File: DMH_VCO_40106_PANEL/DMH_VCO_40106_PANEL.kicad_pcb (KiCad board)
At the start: 2 copper layers, 100 x 200 mm, 35 parts, among them J1 GND

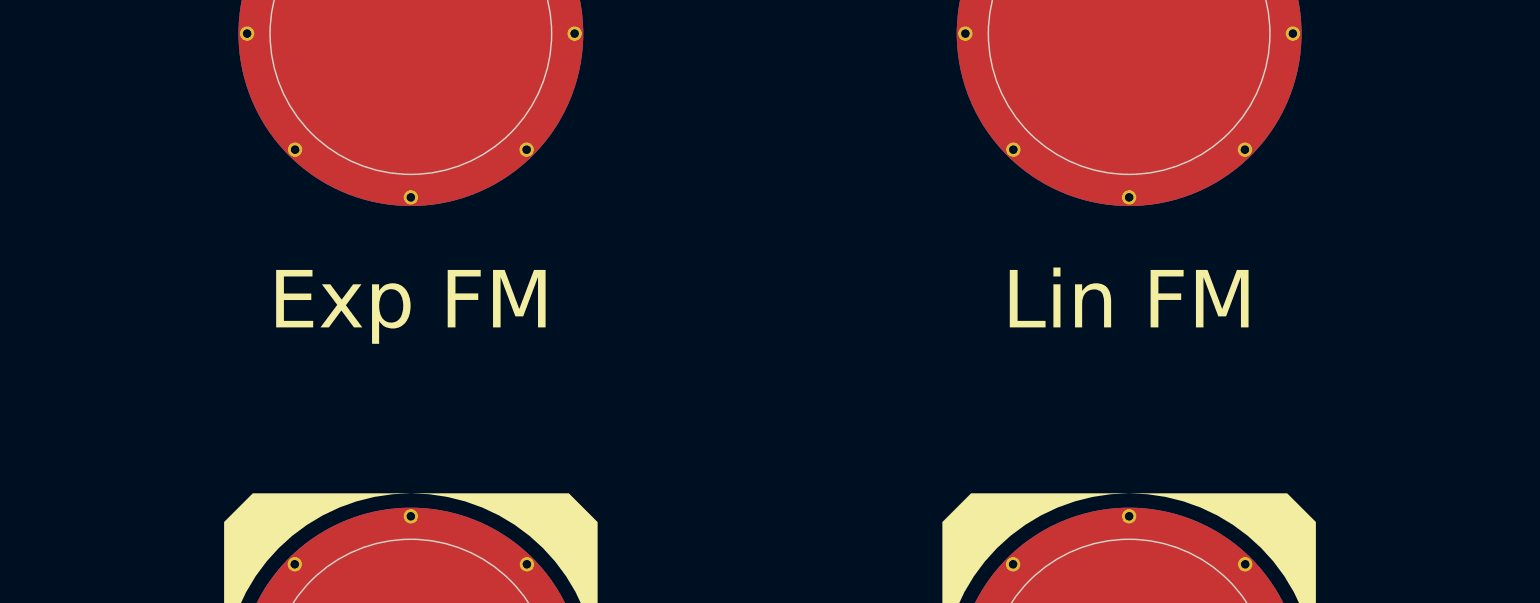
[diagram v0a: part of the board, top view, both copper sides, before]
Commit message: Updates from testing on breadboard
- Removed Bus CV input, normalled it to V/oct input jack instead
- Renamed Lin FM input to Exp FM In 2
- Added annotations about temporary resistor/pot values
- Added annotations about pots and trimpots pinout
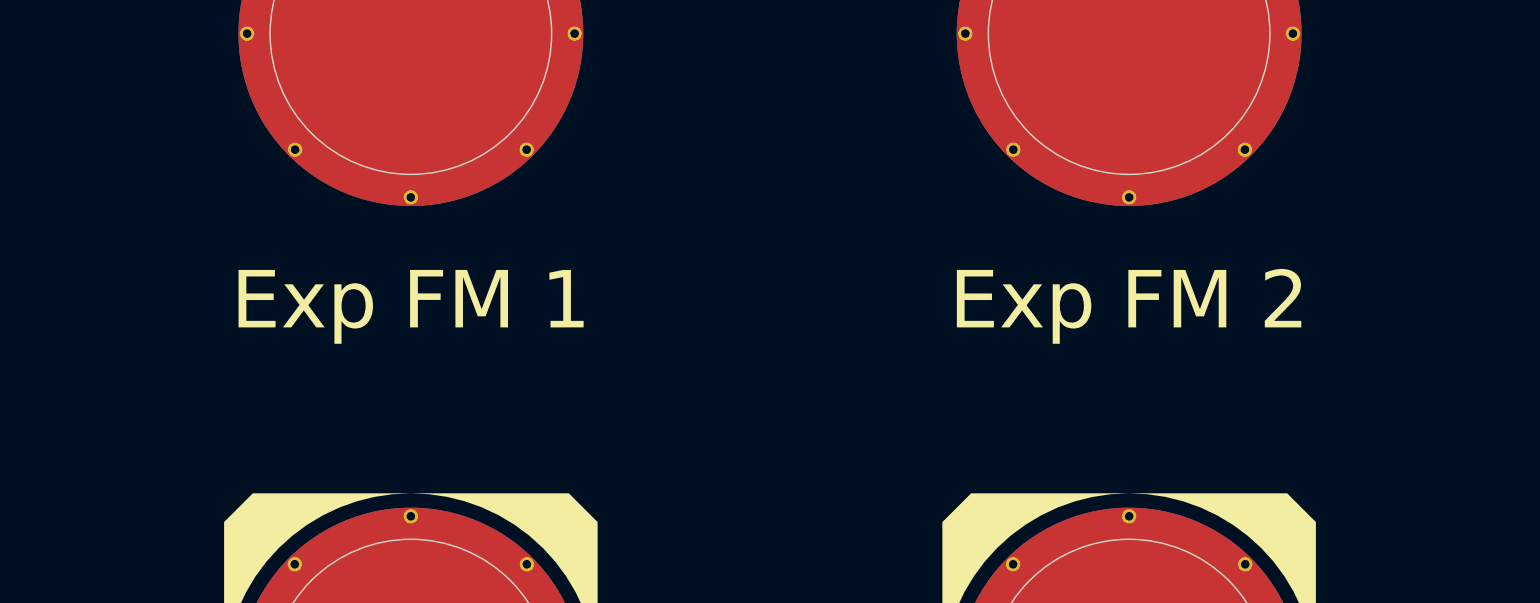
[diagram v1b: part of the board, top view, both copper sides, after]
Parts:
- H10, H18: value Exp FM -> Exp FM 1
- H11, H19: value Lin FM -> Exp FM 2

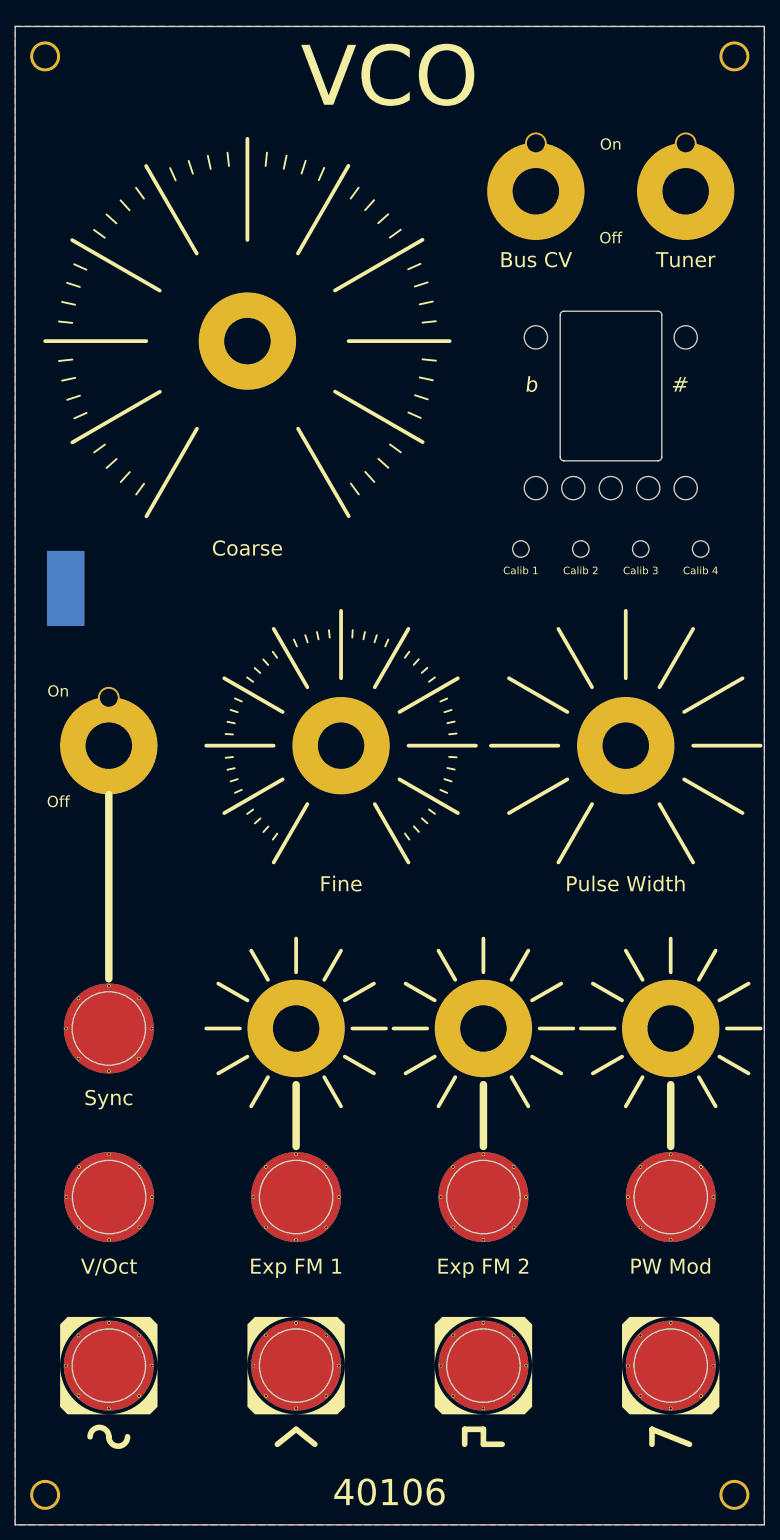
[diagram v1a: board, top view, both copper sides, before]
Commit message: Updated pot mounting hole sizes
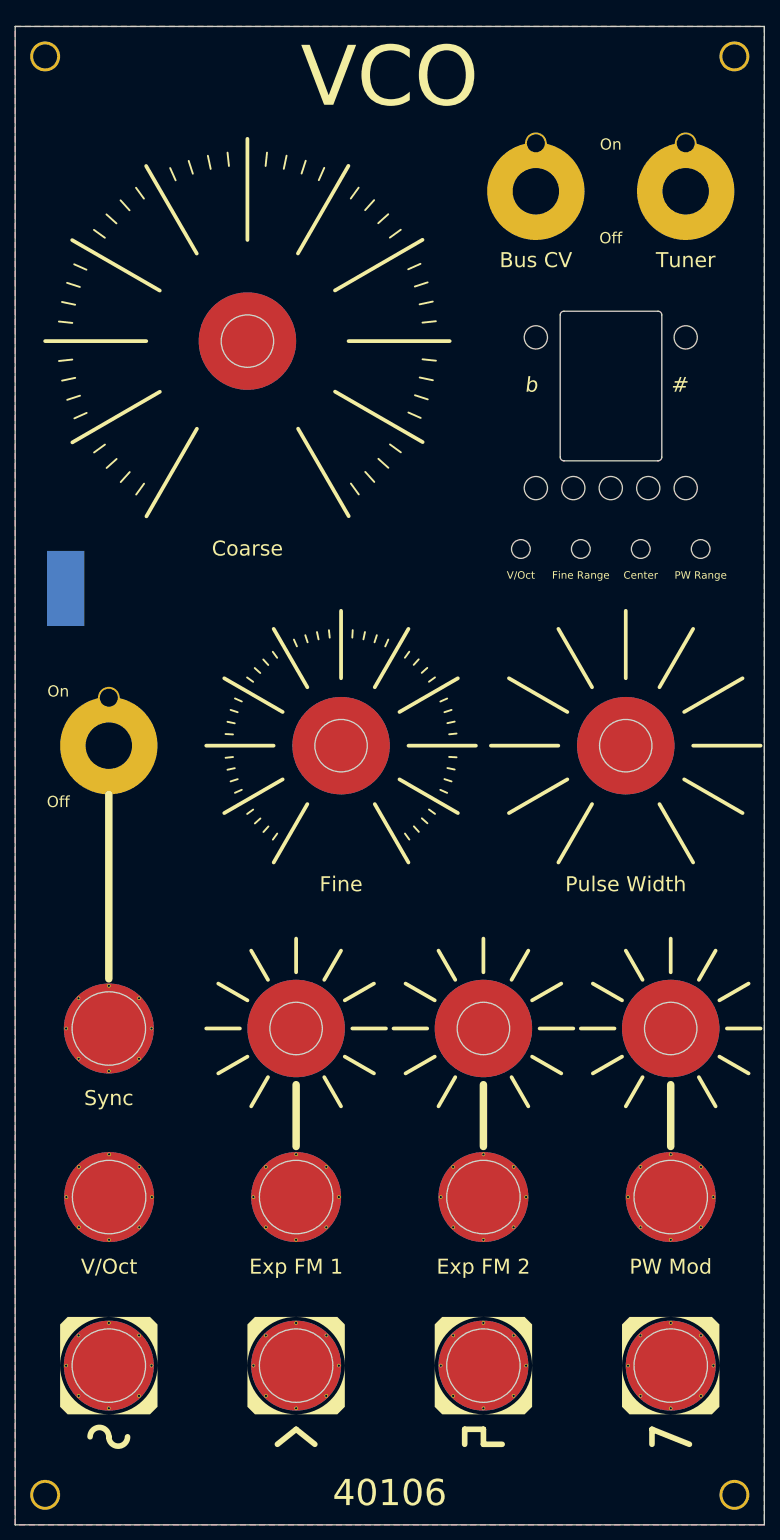
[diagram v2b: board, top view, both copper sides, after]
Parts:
- H21: value Calib 1 -> V/Oct; footprint MountingHole:MountingHole_2.2mm_M2_DIN965 -> MountingHole:MountingHole_2.5mm
- H22: value Calib 2 -> Fine Range; footprint MountingHole:MountingHole_2.2mm_M2_DIN965 -> MountingHole:MountingHole_2.5mm
- H23: value Calib 3 -> Center; footprint MountingHole:MountingHole_2.2mm_M2_DIN965 -> MountingHole:MountingHole_2.5mm
- H24: value Calib 4 -> PW Range; footprint MountingHole:MountingHole_2.2mm_M2_DIN965 -> MountingHole:MountingHole_2.5mm
